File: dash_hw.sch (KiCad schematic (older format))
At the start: 16 parts, among them J1 Conn_01x04, Q1 DMP3056L-7, U1 LM1117-3.3, U2 LM2596S-5

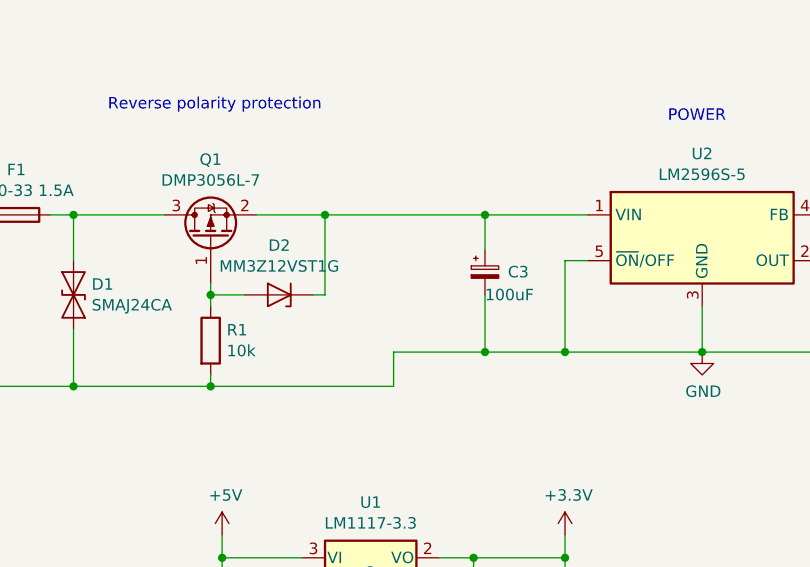
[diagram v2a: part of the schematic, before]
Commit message: one more input capacitor
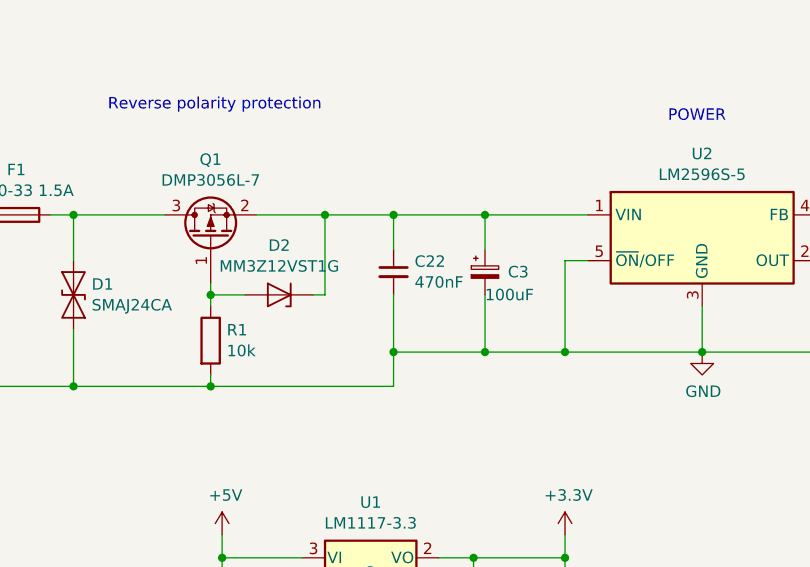
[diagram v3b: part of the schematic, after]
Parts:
- added C22: 470nF, Capacitor_SMD:C_1206_3216Metric, symbol Device:C_Small
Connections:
- net GND: now also C22.2
- net at C3.1, D2.1 (K), Q1.2 (S)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: now also C22.1
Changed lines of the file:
@@
 Connection ~ 2950 5150
 Wire Wire Line
-	2950 5150 3650 5150
+	2950 5150 3250 5150
 Wire Wire Line
 	2600 5500 2450 5500
@@
 Wire Wire Line
 	1500 2650 1650 2650
+$Comp
+L Device:C_Small C?
+U 1 1 5FFB0B2D
+P 3250 5400
+AR Path="/61C146B0/5FFB0B2D" Ref="C?"  Part="1"
+AR Path="/5FFB0B2D" Ref="C22"  Part="1"
+F 0 "C22" H 3342 5446 50  0000 L CNN
+F 1 "470nF" H 3342 5355 50  0000 L CNN
+F 2 "Capacitor_SMD:C_1206_3216Metric" H 3250 5400 50  0001 C CNN
+F 3 "~" H 3250 5400 50  0001 C CNN
+	1    3250 5400
+	1    0    0    -1
+$EndComp
+Wire Wire Line
+	3250 5300 3250 5150
+Connection ~ 3250 5150
+Wire Wire Line
+	3250 5150 3650 5150
+Wire Wire Line
+	3250 5500 3250 5750
+Connection ~ 3250 5750
 $EndSCHEMATC

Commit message: Hardware update Approved
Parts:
- added F2: Polyfuse, Fuse:Fuse_2010_5025Metric, symbol Device:Polyfuse
- added J4: Conn_01x06_Female, Connector_PinHeader_2.54mm:PinHeader_1x06_P2.54mm_Vertical, symbol Connector:Conn_01x06_Female
- C3, C5: footprint Capacitor_SMD:CP_Elec_8x10 -> Capacitor_THT:CP_Radial_D6.3mm_P2.50mm
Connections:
- net CAN- is gone; now on net CANL: J1.3 (Pin_3)
- net +5V: now also F2.2
- new net 5Vfused: F2.1
- new net FAULT1: J4.1 (Pin_1)
- new net FAULT2: J4.2 (Pin_2)
- new net FAULT3: J4.3 (Pin_3)
- new net FAULT4: J4.4 (Pin_4)
- new net FAULT5: J4.5 (Pin_5)
- new net FAULT6: J4.6 (Pin_6)
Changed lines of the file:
@@
 EESchema Schematic File Version 4
+LIBS:dash_hw-cache
 EELAYER 30 0
 EELAYER END
@@
 F6 "E" I L 6000 1550 50
 F7 "RS" I L 6000 1450 50
-$EndSheet
-$Sheet
-S 1650 1600 650  400
-U 61EF75E6
-F0 "Rev" 50
-F1 "Rev.sch" 50
-F2 "SER" I L 1650 1700 50
-F3 "SRCLK" I L 1650 1800 50
-F4 "RCLK" I L 1650 1900 50
-F5 "QH'" O R 2300 1800 50
 $EndSheet
 $Sheet
@@
 Wire Wire Line
 	5350 1950 6000 1950
-Wire Wire Line
-	2400 1050 2500 1050
-Wire Wire Line
-	2500 1050 2500 1450
-Wire Wire Line
-	2500 1450 1600 1450
-Wire Wire Line
-	1600 1450 1600 1700
 Text Label 4300 2500 2    50   ~ 0
 SPI_1_MOSI
@@
 	1200 950  1650 950
 Wire Wire Line
-	1200 1050 1400 1050
-Wire Wire Line
-	1200 1150 1500 1150
-Wire Wire Line
-	1500 1150 1500 1900
-Wire Wire Line
-	1500 1900 1650 1900
-Connection ~ 1500 1150
-Wire Wire Line
-	1500 1150 1650 1150
-Wire Wire Line
-	1600 1700 1650 1700
-Wire Wire Line
 	1500 3450 1650 3450
 Wire Wire Line
@@
 Wire Wire Line
 	1650 3350 1400 3350
-Connection ~ 1400 1050
-Wire Wire Line
-	1400 1050 1650 1050
-Wire Wire Line
-	1650 1800 1400 1800
-Wire Wire Line
-	1400 1800 1400 1050
 $Comp
 L Regulator_Switching:LM2596S-5 U?
@@
 F 0 "C3" H 3750 5400 50  0000 L CNN
 F 1 "100uF" H 3650 5300 50  0000 L CNN
-F 2 "Capacitor_SMD:CP_Elec_8x10" H 3650 5400 50  0001 C CNN
+F 2 "Capacitor_THT:CP_Radial_D6.3mm_P2.50mm" H 3650 5400 50  0001 C CNN
 F 3 "~" H 3650 5400 50  0001 C CNN
 	1    3650 5400
@@
 F 0 "C5" H 6238 5596 50  0000 L CNN
 F 1 "220uF" H 6238 5505 50  0000 L CNN
-F 2 "Capacitor_SMD:CP_Elec_8x10" H 6150 5550 50  0001 C CNN
+F 2 "Capacitor_THT:CP_Radial_D6.3mm_P2.50mm" H 6150 5550 50  0001 C CNN
 F 3 "~" H 6150 5550 50  0001 C CNN
 	1    6150 5550
@@
 CANH
 Text Label 9100 4450 2    50   ~ 0
-CAN-
+CANL
 Text Notes 8800 4050 0    50   ~ 0
 VEHICLE CONNECTOR
@@
 Text Label 1200 1150 2    50   ~ 0
 SPI_1_CS
-NoConn ~ 2300 1800
 Text Label 1200 2450 2    50   ~ 0
 SPI_2_MOSI
@@
 	3250 5500 3250 5750
 Connection ~ 3250 5750
+$Sheet
+S 4950 3150 1100 550
+U 601826D3
+F0 "FAULT_LED" 50
+F1 "Fault_LED.sch" 50
+$EndSheet
+$Comp
+L Connector:Conn_01x06_Female J4
+U 1 1 6018608E
+P 9350 5100
+F 0 "J4" H 9378 5076 50  0000 L CNN
+F 1 "Conn_01x06_Female" H 9378 4985 50  0000 L CNN
+F 2 "Connector_PinHeader_2.54mm:PinHeader_1x06_P2.54mm_Vertical" H 9350 5100 50  0001 C CNN
+F 3 "~" H 9350 5100 50  0001 C CNN
+	1    9350 5100
+	1    0    0    -1
+$EndComp
+Text GLabel 9150 4900 0    50   Input ~ 0
+FAULT1
+Text GLabel 9150 5000 0    50   Input ~ 0
+FAULT2
+Text GLabel 9150 5100 0    50   Input ~ 0
+FAULT3
+Text GLabel 9150 5200 0    50   Input ~ 0
+FAULT4
+Text GLabel 9150 5300 0    50   Input ~ 0
+FAULT5
+Text GLabel 9150 5400 0    50   Input ~ 0
+FAULT6
+$Comp
+L Device:Polyfuse F2
+U 1 1 60187DB8
+P 6750 5350
+F 0 "F2" V 6525 5350 50  0000 C CNN
+F 1 "Polyfuse" V 6616 5350 50  0000 C CNN
+F 2 "Fuse:Fuse_2010_5025Metric" H 6800 5150 50  0001 L CNN
+F 3 "~" H 6750 5350 50  0001 C CNN
+	1    6750 5350
+	0    1    1    0
+$EndComp
+Wire Wire Line
+	6600 5350 6550 5350
+Wire Wire Line
+	6900 5350 7000 5350
+Text GLabel 7000 5350 2    50   Input ~ 0
+5Vfused
+Wire Wire Line
+	1200 1150 1650 1150
+Wire Wire Line
+	1200 1050 1650 1050
+NoConn ~ 2400 1050
 $EndSCHEMATC

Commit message: Updated hardware
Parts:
- removed J1: Conn_01x04, Connector_PinHeader_2.54mm:PinHeader_1x04_P2.54mm_Vertical, symbol Connector_Generic:Conn_01x04
- added J5, J6: Conn_01x02, Connector_PinHeader_2.54mm:PinHeader_1x02_P2.54mm_Vertical, symbol Connector_Generic:Conn_01x02
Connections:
- net CANH: now also J6.1 (Pin_1)
- net CANL: now also J6.2 (Pin_2)
- net GLV+: now also J5.1 (Pin_1)
- net GND: now also J5.2 (Pin_2)
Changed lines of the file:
@@
 GLV-
 NoConn ~ 2300 3350
-$Comp
-L Connector_Generic:Conn_01x04 J1
-U 1 1 5FDE07F9
-P 9300 4350
-F 0 "J1" H 9380 4342 50  0000 L CNN
-F 1 "Conn_01x04" H 9380 4251 50  0000 L CNN
-F 2 "Connector_PinHeader_2.54mm:PinHeader_1x04_P2.54mm_Vertical" H 9300 4350 50  0001 C CNN
-F 3 "~" H 9300 4350 50  0001 C CNN
-	1    9300 4350
-	1    0    0    -1
-$EndComp
-Text Label 9100 4250 2    50   ~ 0
+Text Label 9600 3800 2    50   ~ 0
 GLV+
-Text Label 9100 4550 2    50   ~ 0
+Text Label 9600 3900 2    50   ~ 0
 GLV-
-Text Label 9100 4350 2    50   ~ 0
+Text Label 9600 4050 2    50   ~ 0
 CANH
-Text Label 9100 4450 2    50   ~ 0
+Text Label 9600 4150 2    50   ~ 0
 CANL
-Text Notes 8800 4050 0    50   ~ 0
-VEHICLE CONNECTOR
 $Comp
 L Device:Q_PMOS_GSD Q1
@@
 	1200 1050 1650 1050
 NoConn ~ 2400 1050
+$Comp
+L Connector_Generic:Conn_01x02 J5
+U 1 1 6086EAEA
+P 9800 3800
+F 0 "J5" H 9880 3792 50  0000 L CNN
+F 1 "Conn_01x02" H 9880 3701 50  0000 L CNN
+F 2 "Connector_PinHeader_2.54mm:PinHeader_1x02_P2.54mm_Vertical" H 9800 3800 50  0001 C CNN
+F 3 "~" H 9800 3800 50  0001 C CNN
+	1    9800 3800
+	1    0    0    -1
+$EndComp
+$Comp
+L Connector_Generic:Conn_01x02 J6
+U 1 1 6086F692
+P 9800 4050
+F 0 "J6" H 9880 4042 50  0000 L CNN
+F 1 "Conn_01x02" H 9880 3951 50  0000 L CNN
+F 2 "Connector_PinHeader_2.54mm:PinHeader_1x02_P2.54mm_Vertical" H 9800 4050 50  0001 C CNN
+F 3 "~" H 9800 4050 50  0001 C CNN
+	1    9800 4050
+	1    0    0    -1
+$EndComp
+Text Notes 8000 3700 0    50   ~ 0
+VEHICLE CONNECTOR
 $EndSCHEMATC
